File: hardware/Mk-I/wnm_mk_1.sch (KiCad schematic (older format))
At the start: 34 parts, among them SW1 SW_PUSH, SW10 SW_PUSH, SW11 SW_PUSH, SW12 SW_PUSH, SW13 SW_PUSH, SW14 SW_PUSH, SW15 SW_PUSH, SW16 SW_PUSH, SW18 SW_PUSH, SW19 SW_PUSH, SW2 SW_PUSH, SW20 SW_PUSH, SW21 SW_PUSH, SW22 SW_PUSH, SW3 SW_PUSH, SW4 SW_PUSH, SW5 SW_PUSH, SW6 SW_PUSH, SW7 SW_PUSH, SW8 SW_PUSH, SW9 SW_PUSH, U6 encoder_and_switch, U7 encoder_and_switch

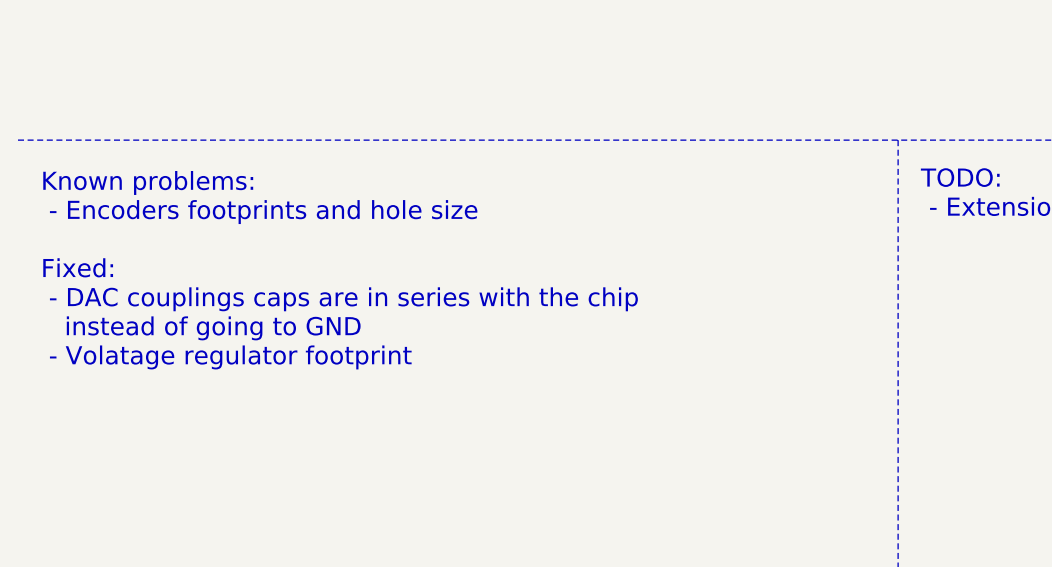
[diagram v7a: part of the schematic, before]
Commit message: HW: Fix encoders footprint
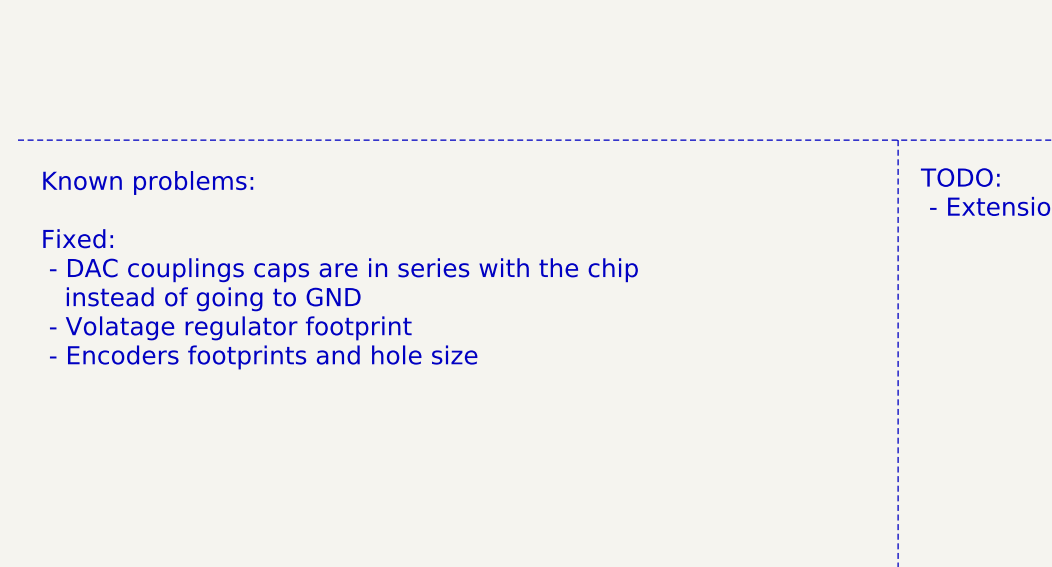
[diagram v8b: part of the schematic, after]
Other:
- note added: "Known problems:\n\nFixed:\n - DAC couplings caps are in series with the chip \n instead of going to GND\n - Volatage regulator footprint\n - Encoders footprints and hole size\n"
- note removed: "Known problems:\n - Encoders footprints and hole size\n\nFixed:\n - DAC couplings caps are in series with the chip \n instead of going to GND\n - Volatage regulator footprint\n"
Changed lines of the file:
@@
 Title "Wee Noise Maker - Mk-I"
 Date ""
-Rev "A"
+Rev "B"
 Comp "Fabien Chouteau"
 Comment1 ""
@@
 	6950 5400 6950 6500
 Text Notes 600  6400 0    79   ~ 0
-Known problems:\n - Encoders footprints and hole size\n\nFixed:\n - DAC couplings caps are in series with the chip \n   instead of going to GND\n - Volatage regulator footprint\n
+Known problems:\n\nFixed:\n - DAC couplings caps are in series with the chip \n   instead of going to GND\n - Volatage regulator footprint\n - Encoders footprints and hole size\n
 $EndSCHEMATC
